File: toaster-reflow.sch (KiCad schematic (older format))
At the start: 22 parts, among them J1 1935161, J2 1935161, J3 Raspberry_Pi_2_3, J4 1935161, J5 1935161, J6 Conn_01x03, K1 1-1415899-3, Q1 Q_PMOS_GSD, Q2 Q_PMOS_GSD, Q3 Q_PMOS_GSD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

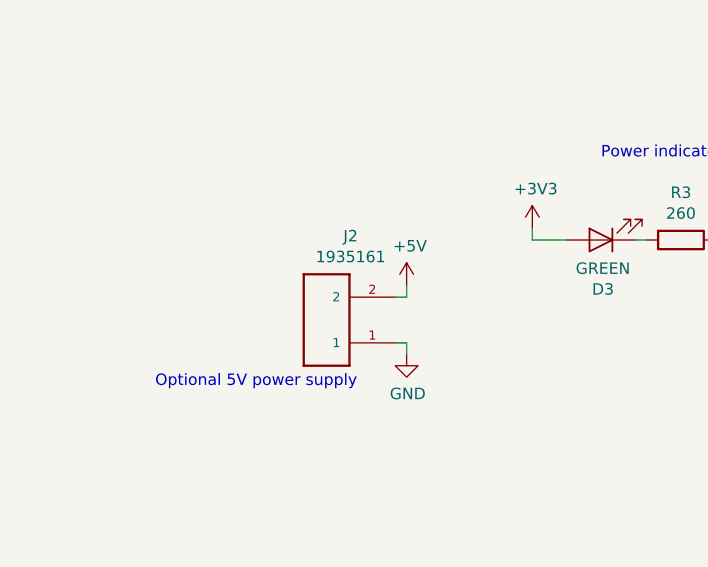
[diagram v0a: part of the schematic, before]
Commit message: Add bom wizard, fix 'duplicate' part
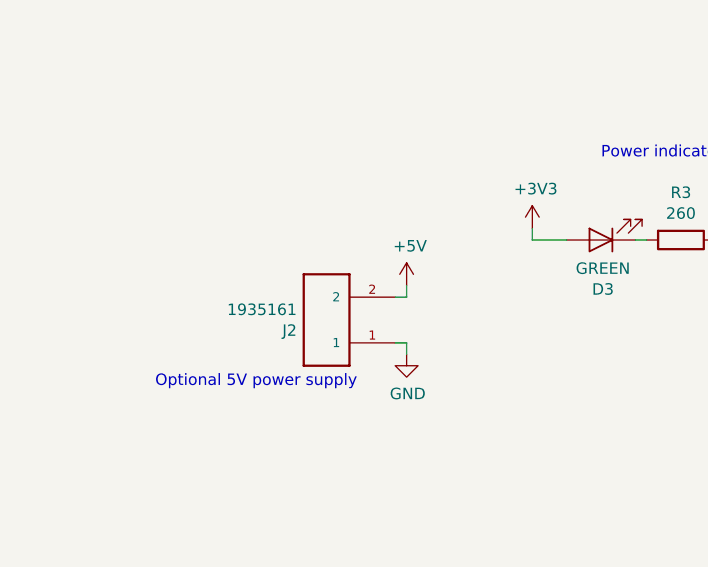
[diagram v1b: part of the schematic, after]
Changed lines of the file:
@@
 EESchema Schematic File Version 4
+LIBS:toaster-reflow-cache
 EELAYER 26 0
 EELAYER END
@@
 $EndComp
 $Comp
-L power:+5V #PWR0101
+L power:+5V #PWR011
 U 1 1 5B8880BA
 P 5300 2500
-F 0 "#PWR0101" H 5300 2350 50  0001 C CNN
+F 0 "#PWR011" H 5300 2350 50  0001 C CNN
 F 1 "+5V" H 5315 2673 50  0000 C CNN
 F 2 "" H 5300 2500 50  0001 C CNN
@@
 	5300 2600 5300 2500
 $Comp
-L power:+3V3 #PWR0102
+L power:+3V3 #PWR012
 U 1 1 5B88815B
 P 5600 2500
-F 0 "#PWR0102" H 5600 2350 50  0001 C CNN
+F 0 "#PWR012" H 5600 2350 50  0001 C CNN
 F 1 "+3V3" H 5615 2673 50  0000 C CNN
 F 2 "" H 5600 2500 50  0001 C CNN
@@
 	5600 2600 5600 2800
 $Comp
-L power:GND #PWR0103
+L power:GND #PWR09
 U 1 1 5B8882CB
 P 5100 5600
-F 0 "#PWR0103" H 5100 5350 50  0001 C CNN
+F 0 "#PWR09" H 5100 5350 50  0001 C CNN
 F 1 "GND" H 5105 5427 50  0000 C CNN
 F 2 "" H 5100 5600 50  0001 C CNN
@@
 $EndComp
 $Comp
-L power:GND #PWR0104
+L power:GND #PWR019
 U 1 1 5B88F2CD
 P 8550 3950
-F 0 "#PWR0104" H 8550 3700 50  0001 C CNN
+F 0 "#PWR019" H 8550 3700 50  0001 C CNN
 F 1 "GND" V 8555 3822 50  0000 R CNN
 F 2 "" H 8550 3950 50  0001 C CNN
@@
 	8650 3950 8550 3950
 $Comp
-L power:+3V3 #PWR0105
+L power:+3V3 #PWR021
 U 1 1 5B88F5EA
 P 8650 3050
-F 0 "#PWR0105" H 8650 2900 50  0001 C CNN
+F 0 "#PWR021" H 8650 2900 50  0001 C CNN
 F 1 "+3V3" H 8665 3223 50  0000 C CNN
 F 2 "" H 8650 3050 50  0001 C CNN
@@
 	2650 5950 2650 6050
 $Comp
-L power:GND #PWR0106
+L power:GND #PWR03
 U 1 1 5B8941DD
 P 2650 6050
-F 0 "#PWR0106" H 2650 5800 50  0001 C CNN
+F 0 "#PWR03" H 2650 5800 50  0001 C CNN
 F 1 "GND" H 2655 5877 50  0000 C CNN
 F 2 "" H 2650 6050 50  0001 C CNN
@@
 $EndComp
 $Comp
-L power:+3V3 #PWR0107
+L power:+3V3 #PWR06
 U 1 1 5B899438
 P 3350 2300
-F 0 "#PWR0107" H 3350 2150 50  0001 C CNN
+F 0 "#PWR06" H 3350 2150 50  0001 C CNN
 F 1 "+3V3" H 3365 2473 50  0000 C CNN
 F 2 "" H 3350 2300 50  0001 C CNN
@@
 	3800 2350 3850 2350
 $Comp
-L power:GND #PWR0108
+L power:GND #PWR08
 U 1 1 5B89AE7E
 P 4200 2400
-F 0 "#PWR0108" H 4200 2150 50  0001 C CNN
+F 0 "#PWR08" H 4200 2150 50  0001 C CNN
 F 1 "GND" H 4205 2227 50  0000 C CNN
 F 2 "" H 4200 2400 50  0001 C CNN
@@
 $EndComp
 $Comp
-L power:GND #PWR0109
+L power:GND #PWR020
 U 1 1 5B8A390C
 P 8550 5300
-F 0 "#PWR0109" H 8550 5050 50  0001 C CNN
+F 0 "#PWR020" H 8550 5050 50  0001 C CNN
 F 1 "GND" V 8555 5172 50  0000 R CNN
 F 2 "" H 8550 5300 50  0001 C CNN
@@
 	8650 5300 8550 5300
 $Comp
-L power:+3V3 #PWR0110
+L power:+3V3 #PWR022
 U 1 1 5B8A3913
 P 8650 4400
-F 0 "#PWR0110" H 8650 4250 50  0001 C CNN
+F 0 "#PWR022" H 8650 4250 50  0001 C CNN
 F 1 "+3V3" H 8665 4573 50  0000 C CNN
 F 2 "" H 8650 4400 50  0001 C CNN
@@
 	2800 5550 2650 5550
 $Comp
-L power:GND #PWR0111
+L power:GND #PWR07
 U 1 1 5B8C5F28
 P 3500 5500
-F 0 "#PWR0111" H 3500 5250 50  0001 C CNN
+F 0 "#PWR07" H 3500 5250 50  0001 C CNN
 F 1 "GND" H 3505 5327 50  0000 C CNN
 F 2 "" H 3500 5500 50  0001 C CNN
@@
 $EndComp
 $Comp
-L power:GND #PWR0112
+L power:GND #PWR018
 U 1 1 5B8E6AA7
 P 7950 2450
-F 0 "#PWR0112" H 7950 2200 50  0001 C CNN
+F 0 "#PWR018" H 7950 2200 50  0001 C CNN
 F 1 "GND" H 7955 2277 50  0000 C CNN
 F 2 "" H 7950 2450 50  0001 C CNN
@@
 $EndComp
 $Comp
-L power:+5V #PWR0113
+L power:+5V #PWR017
 U 1 1 5B8E6B1A
 P 7950 2150
-F 0 "#PWR0113" H 7950 2000 50  0001 C CNN
+F 0 "#PWR017" H 7950 2000 50  0001 C CNN
 F 1 "+5V" H 7965 2323 50  0000 C CNN
 F 2 "" H 7950 2150 50  0001 C CNN
@@
 Servo Connection
 $Comp
-L 1935161:1935161 J2
-U 1 1 5B8EB85F
-P 2450 2700
-F 0 "J2" H 2345 2333 50  0000 C CNN
-F 1 "1935161" H 2345 2424 50  0000 C CNN
-F 2 "PHOENIX_1935161" H 2450 2700 50  0001 L BNN
-F 3 "https://media.digikey.com/pdf/Data%20Sheets/Phoenix%20Contact%20PDFs/1935161.pdf" H 2450 2700 50  0001 L BNN
-F 4 "277-1667-ND" H 2450 2700 50  0001 C CNN "DigikeyPartNumber"
-F 5 "None" H 2450 2700 50  0001 L BNN "Field4"
-F 6 "Conn Terminal Blocks 2 POS 5mm Solder ST Thru-Hole 16A" H 2450 2700 50  0001 L BNN "Field5"
-F 7 "None" H 2450 2700 50  0001 L BNN "Field6"
-F 8 "1935161" H 2450 2700 50  0001 L BNN "Field7"
-F 9 "Unavailable" H 2450 2700 50  0001 L BNN "Field8"
-	1    2450 2700
-	-1   0    0    1
-$EndComp
-$Comp
-L power:+5V #PWR0114
+L power:+5V #PWR04
 U 1 1 5B8ECBEC
 P 2800 2550
-F 0 "#PWR0114" H 2800 2400 50  0001 C CNN
+F 0 "#PWR04" H 2800 2400 50  0001 C CNN
 F 1 "+5V" H 2815 2723 50  0000 C CNN
 F 2 "" H 2800 2550 50  0001 C CNN
@@
 	2800 2600 2800 2550
 $Comp
-L power:GND #PWR0115
+L power:GND #PWR05
 U 1 1 5B8EDFFD
 P 2800 2850
-F 0 "#PWR0115" H 2800 2600 50  0001 C CNN
+F 0 "#PWR05" H 2800 2600 50  0001 C CNN
 F 1 "GND" H 2805 2677 50  0000 C CNN
 F 2 "" H 2800 2850 50  0001 C CNN
@@
 Connection ~ 5250 6600
 $Comp
-L power:+3V3 #PWR0117
+L power:+3V3 #PWR010
 U 1 1 5B92DA54
 P 5250 6200
-F 0 "#PWR0117" H 5250 6050 50  0001 C CNN
+F 0 "#PWR010" H 5250 6050 50  0001 C CNN
 F 1 "+3V3" H 5265 6373 50  0000 C CNN
 F 2 "" H 5250 6200 50  0001 C CNN
@@
 $EndComp
 $Comp
-L power:+3V3 #PWR0118
+L power:+3V3 #PWR01
 U 1 1 5B93CF55
 P 2300 4650
-F 0 "#PWR0118" H 2300 4500 50  0001 C CNN
+F 0 "#PWR01" H 2300 4500 50  0001 C CNN
 F 1 "+3V3" H 2315 4823 50  0000 C CNN
 F 2 "" H 2300 4650 50  0001 C CNN
@@
 $EndComp
 $Comp
-L power:+3V3 #PWR0119
+L power:+3V3 #PWR02
 U 1 1 5B93CFAD
 P 2650 4800
-F 0 "#PWR0119" H 2650 4650 50  0001 C CNN
+F 0 "#PWR02" H 2650 4650 50  0001 C CNN
 F 1 "+3V3" H 2665 4973 50  0000 C CNN
 F 2 "" H 2650 4800 50  0001 C CNN
@@
 $EndComp
 $Comp
-L power:GND #PWR0116
+L power:GND #PWR014
 U 1 1 5B99C32D
 P 5600 7300
-F 0 "#PWR0116" H 5600 7050 50  0001 C CNN
+F 0 "#PWR014" H 5600 7050 50  0001 C CNN
 F 1 "GND" H 5605 7127 50  0000 C CNN
 F 2 "" H 5600 7300 50  0001 C CNN
@@
 	6350 4900 6300 4900
 $Comp
-L power:+3V3 #PWR0120
+L power:+3V3 #PWR013
 U 1 1 5B9AF703
 P 5600 6350
-F 0 "#PWR0120" H 5600 6200 50  0001 C CNN
+F 0 "#PWR013" H 5600 6200 50  0001 C CNN
 F 1 "+3V3" H 5615 6523 50  0000 C CNN
 F 2 "" H 5600 6350 50  0001 C CNN
@@
 Connection ~ 6950 1900
 $Comp
-L power:+3V3 #PWR01
+L power:+3V3 #PWR015
 U 1 1 5B9CED9C
 P 6950 1500
-F 0 "#PWR01" H 6950 1350 50  0001 C CNN
+F 0 "#PWR015" H 6950 1350 50  0001 C CNN
 F 1 "+3V3" H 6965 1673 50  0000 C CNN
 F 2 "" H 6950 1500 50  0001 C CNN
@@
 $EndComp
 $Comp
-L power:+3V3 #PWR02
+L power:+3V3 #PWR016
 U 1 1 5B9CEDA2
 P 7300 1650
-F 0 "#PWR02" H 7300 1500 50  0001 C CNN
+F 0 "#PWR016" H 7300 1500 50  0001 C CNN
 F 1 "+3V3" H 7315 1823 50  0000 C CNN
 F 2 "" H 7300 1650 50  0001 C CNN
@@
 	1    0    0    -1
 $EndComp
+$Comp
+L 1935161:1935161 J2
+U 1 1 5B89EEA8
+P 2450 2700
+F 0 "J2" H 2580 2746 50  0000 L CNN
+F 1 "1935161" H 2580 2655 50  0000 L CNN
+F 2 "PHOENIX_1935161" H 2450 2700 50  0001 L BNN
+F 3 "Phoenix Contact" H 2450 2700 50  0001 L BNN
+F 4 "None" H 2450 2700 50  0001 L BNN "Field4"
+F 5 "Conn Terminal Blocks 2 POS 5mm Solder ST Thru-Hole 16A" H 2450 2700 50  0001 L BNN "Field5"
+F 6 "None" H 2450 2700 50  0001 L BNN "Field6"
+F 7 "1935161" H 2450 2700 50  0001 L BNN "Field7"
+F 8 "Unavailable" H 2450 2700 50  0001 L BNN "Field8"
+F 9 "277-1667-ND" H 2450 2700 50  0001 C CNN "DigikeyPartNumber"
+	1    2450 2700
+	-1   0    0    1
+$EndComp
 $EndSCHEMATC

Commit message: Use better MAX31856, fill in some parts
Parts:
- removed J4, J5: 1935161, PHOENIX_1935161, symbol 1935161:1935161
- removed U1, U2: MAX31855KASA, Package_SO:SOIC-8_3.9x4.9mm_P1.27mm, symbol Sensor_Temperature:MAX31855KASA
- added C1: 0.1uF, Capacitors_SMD:C_0603, symbol Device:C
- added U1: 3.3V Ref, TO_SOT_Packages_SMD:SOT-23, symbol Reference_Voltage:ISL21070CIH320Z-TK
- J1, J2: footprint PHOENIX_1935161 -> 1935161:PHOENIX_1935161
- K1: footprint RELAY_1-1415899-3 -> 1-1415899-3:RELAY_1-1415899-3
- LS1: footprint (none) -> PS12:PS12; DigikeyPartNumber (none) -> 445-2525-1-ND
- Q1, Q2, Q3: footprint (none) -> TO_SOT_Packages_SMD:SOT-23; DigikeyPartNumber (none) -> NTR5105PT1GOSCT-ND
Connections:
- net labels added: +3.3VADC, THERMO1_DRDY, THERMO1_FAULT, THERMO2_DRDY, THERMO2_FAULT, THERMO_MOSI
- wire segments 99 -> 113
- no-connect marks 21 -> 16
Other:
- note added: "Reference voltage for thermocouple circuits"
- note removed: "Thermocouple 1"
- note removed: "Thermocouple 2"

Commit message: Add pcb, update packages
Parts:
- C1: footprint Capacitors_SMD:C_0603 -> Capacitor_SMD:C_0603_1608Metric
- D1: footprint Diodes_SMD:D_SMA -> Diode_SMD:D_SMA
- D2, D3: footprint Diodes_SMD:D_0603 -> Diode_SMD:D_0603_1608Metric
- J3: footprint Pin_Headers:Pin_Header_Straight_2x20_Pitch2.54mm -> Connector_PinHeader_2.54mm:PinHeader_2x20_P2.54mm_Vertical
- J6: footprint Pin_Headers:Pin_Header_Straight_1x02_Pitch2.54mm -> Connector_PinSocket_2.54mm:PinSocket_1x02_P2.54mm_Vertical
- Q1, Q2, Q3, U1: footprint TO_SOT_Packages_SMD:SOT-23 -> Package_TO_SOT_SMD:SOT-23
- R1, R2, R3, R4, R5, R6: footprint Resistors_SMD:R_0603 -> Resistor_SMD:R_0603_1608Metric
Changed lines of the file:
@@
 F 2 "1-1415899-3:RELAY_1-1415899-3" H 2150 5750 50  0001 L BNN
 F 3 "TE Connectivity" H 2150 5750 50  0001 L BNN
-F 4 "Electromechanical Relay 5VDC 60Ohm 16A SPST-NO _29x12.7x15.7_mm THT Power Relay" H 2150 5750 50  0001 L BNN "Field4"
-F 5 "http://www.te.com/usa-en/product-1-1415899-3.html" H 2150 5750 50  0001 L BNN "Field5"
-F 6 "1-1415899-3" H 2150 5750 50  0001 L BNN "Field6"
-F 7 "None" H 2150 5750 50  0001 L BNN "Field7"
-F 8 "Compliant" H 2150 5750 50  0001 L BNN "Field10"
-F 9 "PB1267-ND" H 2150 5750 50  0001 C CNN "DigikeyPartNumber"
+F 4 "PB1267-ND" H 2150 5750 50  0001 C CNN "DigikeyPartNumber"
+F 5 "Electromechanical Relay 5VDC 60Ohm 16A SPST-NO _29x12.7x15.7_mm THT Power Relay" H 2150 5750 50  0001 L BNN "Field4"
+F 6 "http://www.te.com/usa-en/product-1-1415899-3.html" H 2150 5750 50  0001 L BNN "Field5"
+F 7 "1-1415899-3" H 2150 5750 50  0001 L BNN "Field6"
+F 8 "None" H 2150 5750 50  0001 L BNN "Field7"
+F 9 "Compliant" H 2150 5750 50  0001 L BNN "Field10"
 	1    2150 5750
 	-1   0    0    1
@@
 F 0 "D3" H 3641 2566 50  0000 C CNN
 F 1 "GREEN" H 3641 2475 50  0000 C CNN
-F 2 "Diodes_SMD:D_0603" H 3650 2350 50  0001 C CNN
+F 2 "Diode_SMD:D_0603_1608Metric" H 3650 2350 50  0001 C CNN
 F 3 "https://katalog.we-online.de/led/datasheet/150060VS75000.pdf" H 3650 2350 50  0001 C CNN
 F 4 "732-4980-1-ND" H 3650 2350 50  0001 C CNN "DigikeyPartNumber"
@@
 F 0 "R3" V 3793 2350 50  0000 C CNN
 F 1 "260" V 3884 2350 50  0000 C CNN
-F 2 "Resistors_SMD:R_0603" V 3930 2350 50  0001 C CNN
+F 2 "Resistor_SMD:R_0603_1608Metric" V 3930 2350 50  0001 C CNN
 F 3 "https://industrial.panasonic.com/cdbs/www-data/pdf/RDA0000/AOA0000C304.pdf" H 4000 2350 50  0001 C CNN
 F 4 "P261HCT-ND" V 4000 2350 50  0001 C CNN "DigikeyPartNumber"
@@
 F 0 "D2" H 2942 5295 50  0000 C CNN
 F 1 "RED" H 2942 5386 50  0000 C CNN
-F 2 "Diodes_SMD:D_0603" H 2950 5550 50  0001 C CNN
+F 2 "Diode_SMD:D_0603_1608Metric" H 2950 5550 50  0001 C CNN
 F 3 "https://katalog.we-online.de/led/datasheet/150060RS75000.pdf" H 2950 5550 50  0001 C CNN
 F 4 "732-4978-1-ND" H 2950 5550 50  0001 C CNN "DigikeyPartNumber"
@@
 F 0 "R2" V 3507 5550 50  0000 C CNN
 F 1 "470" V 3416 5550 50  0000 C CNN
-F 2 "Resistors_SMD:R_0603" V 3230 5550 50  0001 C CNN
+F 2 "Resistor_SMD:R_0603_1608Metric" V 3230 5550 50  0001 C CNN
 F 3 "https://industrial.panasonic.com/cdbs/www-data/pdf/RDA0000/AOA0000C304.pdf" H 3300 5550 50  0001 C CNN
 F 4 "P470HCT-ND" H 3300 5550 50  0001 C CNN "DigikeyPartNumber"
@@
 F 0 "J6" H 8280 2342 50  0000 L CNN
 F 1 "Conn_01x03" H 8280 2251 50  0000 L CNN
-F 2 "Pin_Headers:Pin_Header_Straight_1x02_Pitch2.54mm" H 8200 2300 50  0001 C CNN
+F 2 "Connector_PinSocket_2.54mm:PinSocket_1x02_P2.54mm_Vertical" H 8200 2300 50  0001 C CNN
 F 3 "https://katalog.we-online.de/em/datasheet/6130xx11121.pdf" H 8200 2300 50  0001 C CNN
 F 4 "732-5316-ND" H 8200 2300 50  0001 C CNN "DigikeyPartNumber"
@@
 F 0 "R1" H 2370 4896 50  0000 L CNN
 F 1 "10K" H 2370 4805 50  0000 L CNN
-F 2 "Resistors_SMD:R_0603" V 2230 4850 50  0001 C CNN
+F 2 "Resistor_SMD:R_0603_1608Metric" V 2230 4850 50  0001 C CNN
 F 3 "http://industrial.panasonic.com/www-cgi/jvcr13pz.cgi?E+PZ+3+AOA0001+ERJ3GEYJ103V+7+WW" H 2300 4850 50  0001 C CNN
 F 4 "P10KGCT-ND" H 2300 4850 50  0001 C CNN "DigikeyPartNumber"
@@
 F 0 "D1" V 2604 5829 50  0000 L CNN
 F 1 "400V 1A" V 2695 5829 50  0000 L CNN
-F 2 "Diodes_SMD:D_SMA" H 2650 5750 50  0001 C CNN
+F 2 "Diode_SMD:D_SMA" H 2650 5750 50  0001 C CNN
 F 3 "http://www.smc-diodes.com/propdf/S1A-S1M%20N0560%20REV.B.pdf" H 2650 5750 50  0001 C CNN
 F 4 "1655-1504-1-ND" H 2650 5750 50  0001 C CNN "DigikeyPartNumber"
@@
 F 0 "Q2" H 5706 6646 50  0000 L CNN
 F 1 "Q_PMOS_GSD" H 5706 6555 50  0000 L CNN
-F 2 "TO_SOT_Packages_SMD:SOT-23" H 5700 6700 50  0001 C CNN
+F 2 "Package_TO_SOT_SMD:SOT-23" H 5700 6700 50  0001 C CNN
 F 3 "http://www.onsemi.com/pub/Collateral/NTR5105P-D.PDF" H 5500 6600 50  0001 C CNN
 F 4 "NTR5105PT1GOSCT-ND" H 5500 6600 50  0001 C CNN "DigikeyPartNumber"
@@
 F 0 "R4" H 5320 6446 50  0000 L CNN
 F 1 "10K" H 5320 6355 50  0000 L CNN
-F 2 "Resistors_SMD:R_0603" V 5180 6400 50  0001 C CNN
+F 2 "Resistor_SMD:R_0603_1608Metric" V 5180 6400 50  0001 C CNN
 F 3 "http://industrial.panasonic.com/www-cgi/jvcr13pz.cgi?E+PZ+3+AOA0001+ERJ3GEYJ103V+7+WW" H 5250 6400 50  0001 C CNN
 F 4 "P10KGCT-ND" H 5250 6400 50  0001 C CNN "DigikeyPartNumber"
@@
 F 0 "R5" H 5670 7096 50  0000 L CNN
 F 1 "1K" H 5670 7005 50  0000 L CNN
-F 2 "Resistors_SMD:R_0603" V 5530 7050 50  0001 C CNN
+F 2 "Resistor_SMD:R_0603_1608Metric" V 5530 7050 50  0001 C CNN
 F 3 "https://www.rohm.com/datasheet/ESR01MZPF/esr-e" H 5600 7050 50  0001 C CNN
 F 4 "RHM1.0KDCT-ND" H 5600 7050 50  0001 C CNN "DigikeyPartNumber"
@@
 F 0 "R6" H 7020 1746 50  0000 L CNN
 F 1 "10K" H 7020 1655 50  0000 L CNN
-F 2 "Resistors_SMD:R_0603" V 6880 1700 50  0001 C CNN
+F 2 "Resistor_SMD:R_0603_1608Metric" V 6880 1700 50  0001 C CNN
 F 3 "http://industrial.panasonic.com/www-cgi/jvcr13pz.cgi?E+PZ+3+AOA0001+ERJ3GEYJ103V+7+WW" H 6950 1700 50  0001 C CNN
 F 4 "P10KGCT-ND" H 6950 1700 50  0001 C CNN "DigikeyPartNumber"
@@
 F 0 "Q1" H 2756 5096 50  0000 L CNN
 F 1 "Q_PMOS_GSD" H 2756 5005 50  0000 L CNN
-F 2 "TO_SOT_Packages_SMD:SOT-23" H 2750 5150 50  0001 C CNN
+F 2 "Package_TO_SOT_SMD:SOT-23" H 2750 5150 50  0001 C CNN
 F 3 "http://www.onsemi.com/pub/Collateral/NTR5105P-D.PDF" H 2550 5050 50  0001 C CNN
 F 4 "NTR5105PT1GOSCT-ND" H 2550 5050 50  0001 C CNN "DigikeyPartNumber"
@@
 F 0 "Q3" H 7406 1946 50  0000 L CNN
 F 1 "Q_PMOS_GSD" H 7406 1855 50  0000 L CNN
-F 2 "TO_SOT_Packages_SMD:SOT-23" H 7400 2000 50  0001 C CNN
+F 2 "Package_TO_SOT_SMD:SOT-23" H 7400 2000 50  0001 C CNN
 F 3 "http://www.onsemi.com/pub/Collateral/NTR5105P-D.PDF" H 7200 1900 50  0001 C CNN
 F 4 "NTR5105PT1GOSCT-ND" H 7200 1900 50  0001 C CNN "DigikeyPartNumber"
@@
 F 0 "U1" H 7870 5696 50  0000 R CNN
 F 1 "3.3V Ref" H 7870 5605 50  0000 R CNN
-F 2 "TO_SOT_Packages_SMD:SOT-23" H 8600 5400 50  0001 C CIN
+F 2 "Package_TO_SOT_SMD:SOT-23" H 8600 5400 50  0001 C CIN
 F 3 "http://www.onsemi.com/pub/Collateral/NCP51460-D.PDF" H 8100 5650 50  0001 C CIN
 F 4 "NCP51460SN33T1GOSCT-ND" H 8100 5650 50  0001 C CNN "DigikeyPartNumber"
@@
 F 0 "J3" H 5500 5578 50  0000 C CNN
 F 1 "Raspberry_Pi_2_3" H 5500 5487 50  0000 C CNN
-F 2 "Pin_Headers:Pin_Header_Straight_2x20_Pitch2.54mm" H 5500 4100 50  0001 C CNN
+F 2 "Connector_PinHeader_2.54mm:PinHeader_2x20_P2.54mm_Vertical" H 5500 4100 50  0001 C CNN
 F 3 "https://www.raspberrypi.org/documentation/hardware/raspberrypi/schematics/rpi_SCH_3bplus_1p0_reduced.pdf" H 5500 4100 50  0001 C CNN
 F 4 "S9200-ND" H 5500 4100 50  0001 C CNN "DigikeyPartNumber"
@@
 F 0 "C1" H 7915 5346 50  0000 L CNN
 F 1 "0.1uF" H 7915 5255 50  0000 L CNN
-F 2 "Capacitors_SMD:C_0603" H 7838 5150 50  0001 C CNN
+F 2 "Capacitor_SMD:C_0603_1608Metric" H 7838 5150 50  0001 C CNN
 F 3 "http://www.samsungsem.com/kr/support/product-search/mlcc/CL10F104ZO8NNNC.jsp" H 7800 5300 50  0001 C CNN
 F 4 "1276-1258-1-ND" H 7800 5300 50  0001 C CNN "DigikeyPartNumber"

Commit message: Forgot a footprint! Created components on board
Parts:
- J6: footprint Connector_PinSocket_2.54mm:PinSocket_1x02_P2.54mm_Vertical -> Connector_PinSocket_2.54mm:PinSocket_1x03_P2.54mm_Vertical
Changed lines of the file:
@@
 F 0 "J6" H 8280 2342 50  0000 L CNN
 F 1 "Conn_01x03" H 8280 2251 50  0000 L CNN
-F 2 "Connector_PinSocket_2.54mm:PinSocket_1x02_P2.54mm_Vertical" H 8200 2300 50  0001 C CNN
+F 2 "Connector_PinSocket_2.54mm:PinSocket_1x03_P2.54mm_Vertical" H 8200 2300 50  0001 C CNN
 F 3 "https://katalog.we-online.de/em/datasheet/6130xx11121.pdf" H 8200 2300 50  0001 C CNN
 F 4 "732-5316-ND" H 8200 2300 50  0001 C CNN "DigikeyPartNumber"

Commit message: Add a bunch of stuff
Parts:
- removed Q1, Q2, Q3: Q_PMOS_GSD, Package_TO_SOT_SMD:SOT-23, symbol Device:Q_PMOS_GSD
- removed R6: 10K, Resistor_SMD:R_0603_1608Metric, symbol Device:R
- added J4: Conn_01x04, 1990025:1990025, symbol Connector_Generic:Conn_01x04
- added Q1, Q2: Q_NMOS_GSD, Package_TO_SOT_SMD:SC-59, symbol Device:Q_NMOS_GSD
- R2: value 470 -> 1K; DigikeyPartNumber P470HCT-ND -> RHM1.0KDCT-ND
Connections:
- wire segments 113 -> 114
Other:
- note added: "Activation indicator\n"
- note added: "Buzzer"
- note added: "Instrument activation relay"
- note removed: "Heating indicator"
- note removed: "Toaster oven relay"
- moved on the sheet: D2, D3, LS1, R3, R4, R5

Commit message: update some stuff
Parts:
- added R?: 1K, Resistor_SMD:R_0603_1608Metric, symbol Device:R
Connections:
- net +3V3: now also LS1.1, R5.1
- net SERVO_PWM: now also R?.1; no longer J6.1 (Pin_1)
- net at K1.11_1 (11), K1.11_2 (11): now also J1.1; no longer J1.2
- net at K1.14_1 (14), K1.14_2 (14): now also J1.2; no longer J1.1
- new net: J6.1 (Pin_1), R?.2
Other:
- moved on the sheet: J1
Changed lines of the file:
@@
 $EndComp
-Wire Wire Line
-	1550 5650 1650 5650
 Wire Wire Line
 	1550 5850 1650 5850
@@
 L 1935161:1935161 J1
 U 1 1 5B8AC1A4
-P 1250 5750
-F 0 "J1" H 1145 5383 50  0000 C CNN
-F 1 "1935161" H 1145 5474 50  0000 C CNN
-F 2 "1935161:PHOENIX_1935161" H 1250 5750 50  0001 L BNN
-F 3 "Phoenix Contact" H 1250 5750 50  0001 L BNN
-F 4 "277-1667-ND" H 1250 5750 50  0001 C CNN "DigikeyPartNumber"
-F 5 "None" H 1250 5750 50  0001 L BNN "Field4"
-F 6 "Conn Terminal Blocks 2 POS 5mm Solder ST Thru-Hole 16A" H 1250 5750 50  0001 L BNN "Field5"
-F 7 "None" H 1250 5750 50  0001 L BNN "Field6"
-F 8 "1935161" H 1250 5750 50  0001 L BNN "Field7"
-F 9 "Unavailable" H 1250 5750 50  0001 L BNN "Field8"
-	1    1250 5750
+P 1100 5550
+F 0 "J1" H 995 5183 50  0000 C CNN
+F 1 "1935161" H 995 5274 50  0000 C CNN
+F 2 "1935161:PHOENIX_1935161" H 1100 5550 50  0001 L BNN
+F 3 "Phoenix Contact" H 1100 5550 50  0001 L BNN
+F 4 "277-1667-ND" H 1100 5550 50  0001 C CNN "DigikeyPartNumber"
+F 5 "None" H 1100 5550 50  0001 L BNN "Field4"
+F 6 "Conn Terminal Blocks 2 POS 5mm Solder ST Thru-Hole 16A" H 1100 5550 50  0001 L BNN "Field5"
+F 7 "None" H 1100 5550 50  0001 L BNN "Field6"
+F 8 "1935161" H 1100 5550 50  0001 L BNN "Field7"
+F 9 "Unavailable" H 1100 5550 50  0001 L BNN "Field8"
+	1    1100 5550
 	-1   0    0    -1
 $EndComp
@@
 	4700 4300 4100 4300
 Wire Wire Line
-	7500 2200 8000 2200
-Text Label 7500 2200 0    50   ~ 0
+	7050 2200 7550 2200
+Text Label 7050 2200 0    50   ~ 0
 SERVO_PWM
 $Comp
@@
 Text Notes 4900 6700 0    50   ~ 0
 Buzzer
+Wire Wire Line
+	1400 5650 1650 5650
+Wire Wire Line
+	1400 5450 1550 5450
+Wire Wire Line
+	1550 5450 1550 5850
+$Comp
+L Device:R R?
+U 1 1 5BE2B437
+P 7700 2200
+F 0 "R?" H 7770 2246 50  0000 L CNN
+F 1 "1K" H 7770 2155 50  0000 L CNN
+F 2 "Resistor_SMD:R_0603_1608Metric" V 7630 2200 50  0001 C CNN
+F 3 "https://www.rohm.com/datasheet/ESR01MZPF/esr-e" H 7700 2200 50  0001 C CNN
+F 4 "RHM1.0KDCT-ND" H 7700 2200 50  0001 C CNN "DigikeyPartNumber"
+	1    7700 2200
+	0    -1   -1   0
+$EndComp
+Wire Wire Line
+	8000 2200 7850 2200
+$Comp
+L power:+3V3 #PWR?
+U 1 1 5BE3EC4D
+P 5300 6250
+F 0 "#PWR?" H 5300 6100 50  0001 C CNN
+F 1 "+3V3" H 5315 6423 50  0000 C CNN
+F 2 "" H 5300 6250 50  0001 C CNN
+F 3 "" H 5300 6250 50  0001 C CNN
+	1    5300 6250
+	1    0    0    -1
+$EndComp
+Connection ~ 5300 6250
 $EndSCHEMATC
